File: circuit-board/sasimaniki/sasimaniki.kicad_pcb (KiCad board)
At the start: 2 copper layers, 94 x 35.6 mm, 12 parts, among them J2 Conn_01x02_Socket, J3 Conn_01x03_Socket, J4 Conn_01x05_Pin, U1 AE-ESP32-WROOM-32E-MINI, U2 AE-LXDC55-5V

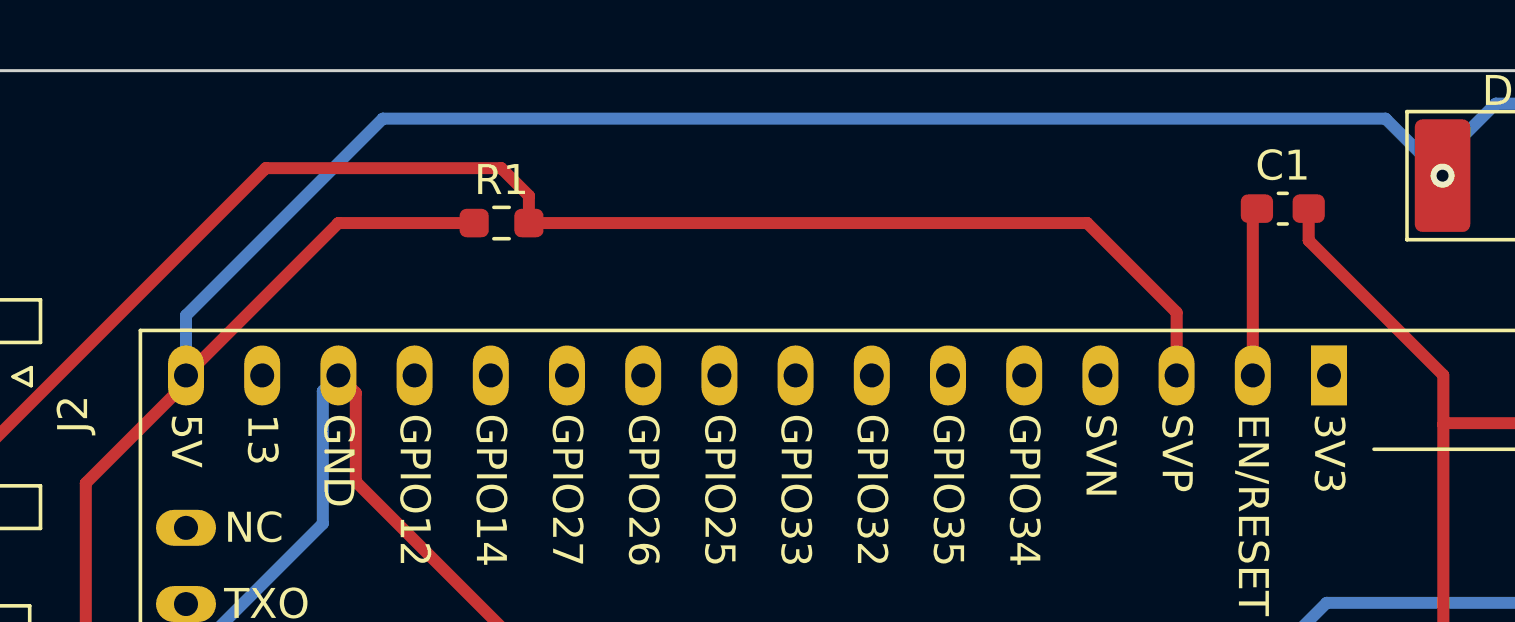
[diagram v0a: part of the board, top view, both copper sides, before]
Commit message: update "measure" circuit board.
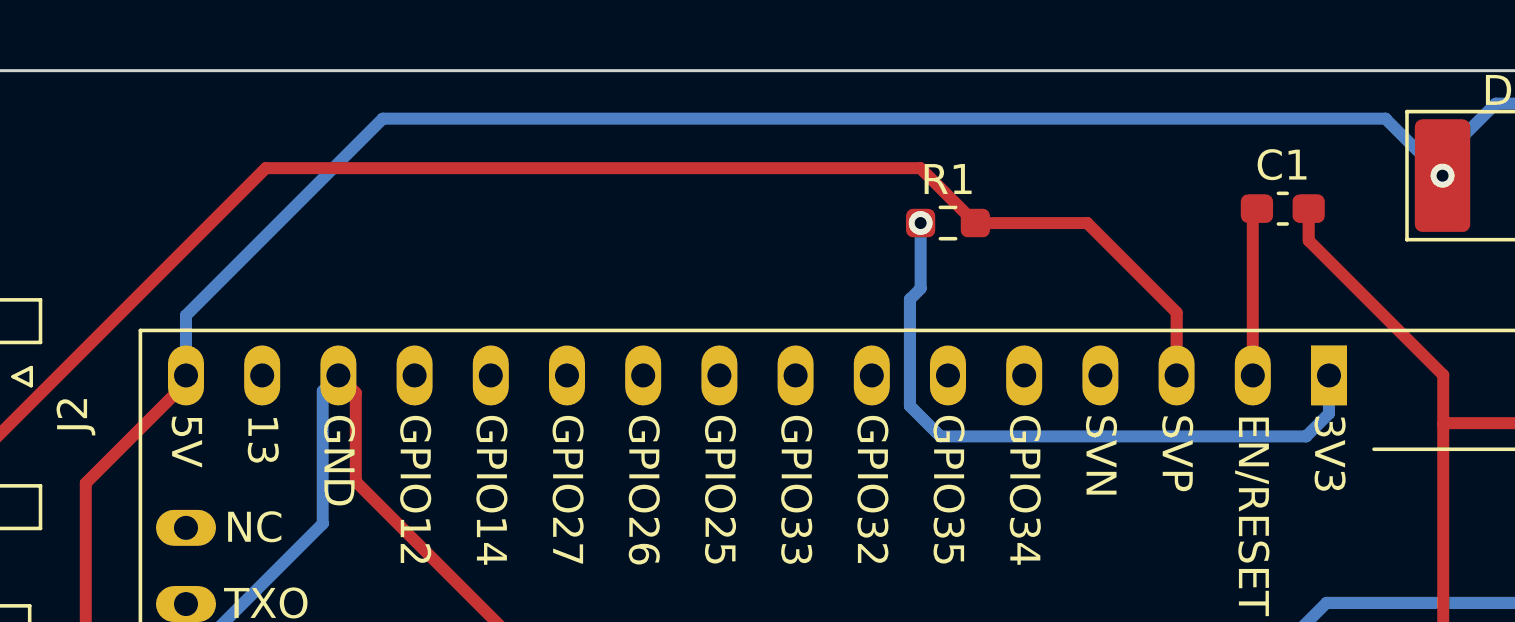
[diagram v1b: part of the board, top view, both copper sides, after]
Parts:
- moved R1 14.9 mm to (142.2, 68.6)
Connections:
- R1 pad 1: +5V -> +3V3
- U1 pad 1: unconnected-(U1-3V3-Pad1) -> +3V3
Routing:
- net +3V3: track 0.00 -> 22.2 mm, vias 0 -> 1
- net +5V: track 111.8 -> 100.0 mm
- net /SENSE: track 48.8 -> 48.3 mm
